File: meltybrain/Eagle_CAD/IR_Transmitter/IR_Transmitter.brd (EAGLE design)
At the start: 41 x 31 mm, 14 parts, among them J1 AVR_SPI_PROG_3X2NS, Q1 BSS806N, Q2 FDN352AP, U1 LMH6612MAX/NOPB, U2 AP2210K-5.0TRG1

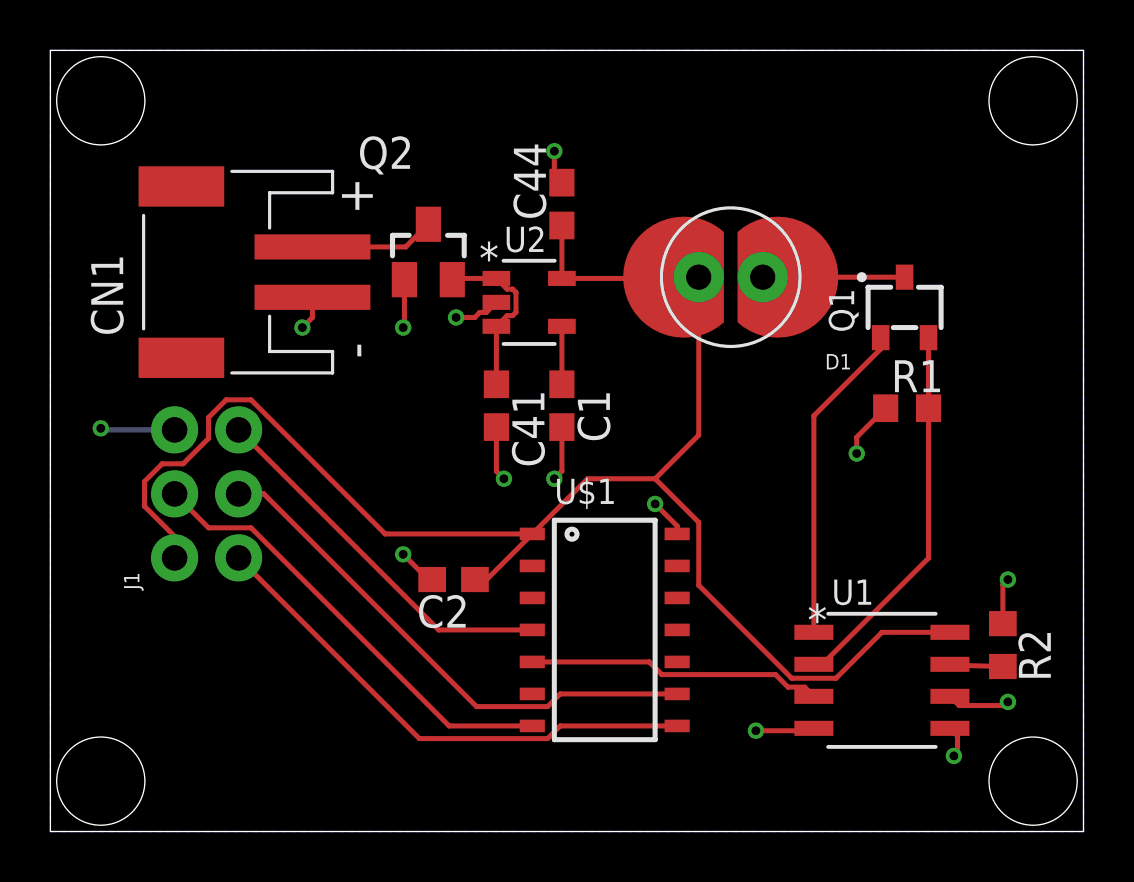
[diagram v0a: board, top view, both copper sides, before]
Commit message: Diode Lobes Removed, Board Shrunk
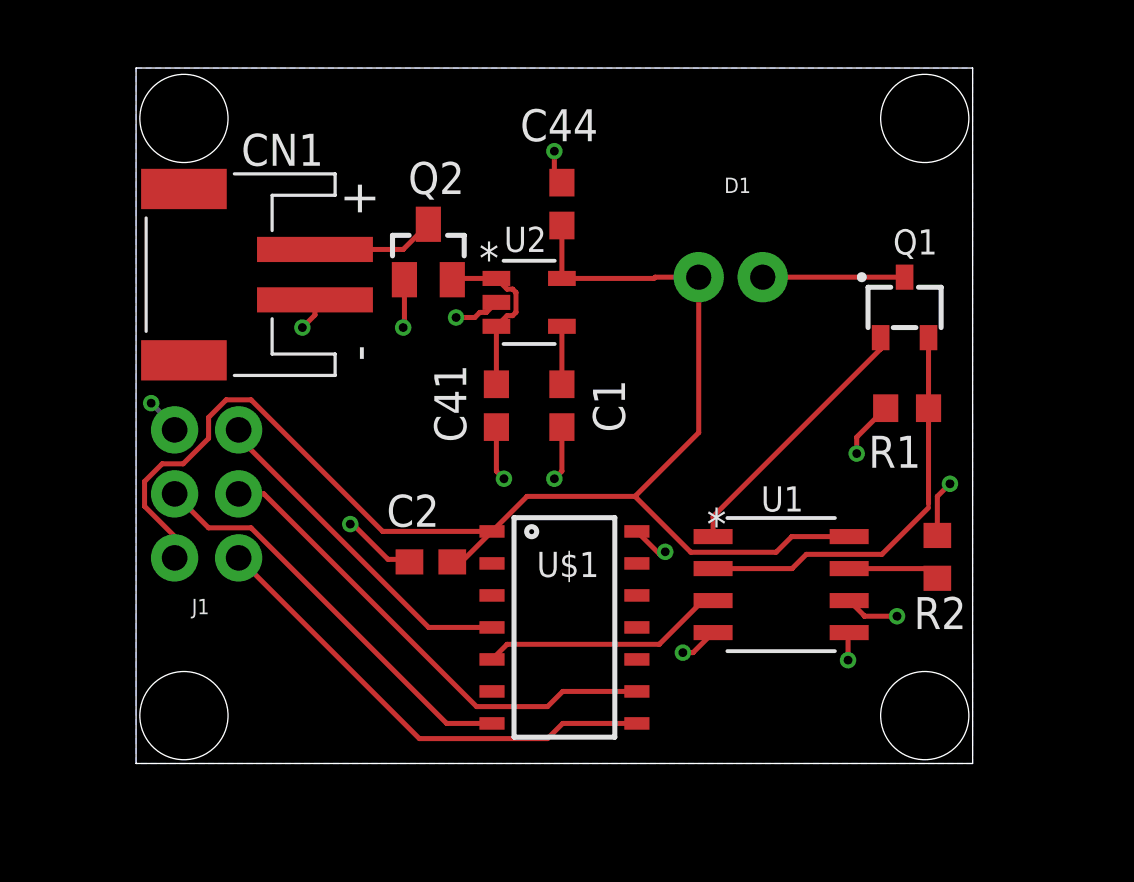
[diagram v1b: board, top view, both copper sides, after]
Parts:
- moved U1 5.52 mm to (27.0, 7.80)
- moved R2 4.36 mm to (33.2, 8.90)
- moved U$1 1.60 mm to (18.4, 6.10)
- moved C2 1.14 mm to (13.1, 8.70)
- moved CN1 0.14 mm to (4.80, 20.1)
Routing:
- net +5V: track 65.2 -> 56.6 mm
- net N$2: track 12.8 -> 10.6 mm
- net OUT: track 11.7 -> 9.74 mm
- net N$3: track 2.12 -> 3.88 mm
- net MOSI: track 18.0 -> 16.4 mm
- net SCK: track 21.1 -> 19.6 mm
- net MISO: track 20.6 -> 19.0 mm
- net RST: track 14.9 -> 13.5 mm
- net N$1: track 15.0 -> 16.3 mm
- net GND: track 27.4 -> 26.2 mm
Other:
- board size 41 x 31 mm -> 33.2 x 27.6 mm
